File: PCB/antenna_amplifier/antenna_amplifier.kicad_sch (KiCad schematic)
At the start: 0 parts

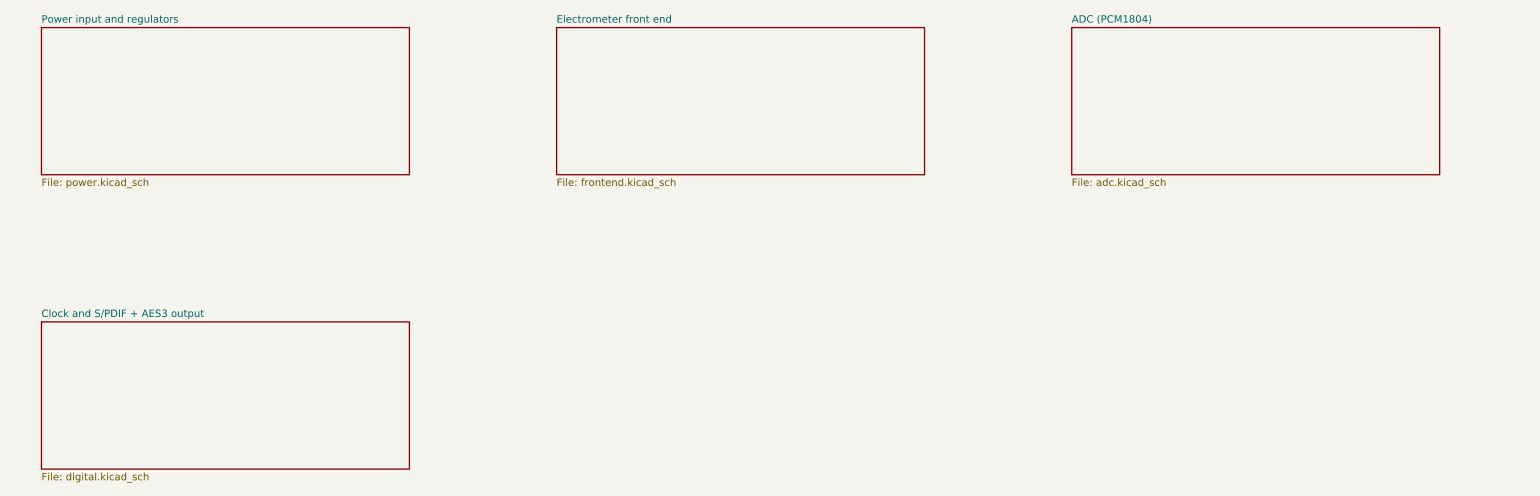
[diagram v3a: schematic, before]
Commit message: Pedantic schematic and silkscreen pass: zero overlaps, labels clear of tracks
Schematics
- tools/kicadgen/schcheck.py checks KiCad's own SVG rendering (exact stroke boxes)
  for text over text, lines through text, crowded twin labels and text outside the
  frame. Both schematics: 0 findings; ERC 0 on both.
- Generator: Sheet.join (one wire + one label instead of two facing labels),
  per-symbol field positions, per-pin stub lengths, shared power symbol for
  adjacent top/bottom rail pins, crowded rail runs get one label, longer PCM1804
  pins (no-connect cross clear of the pin number), PE value clear of its symbol.
- Fixed: doubled VIN_RAW/BIAS_DIV/LED_OVF/CV_ADJ/LED_C labels, +5VA vs VREG,
  +5V_PRE twins, CS8406 GND straps vs neighbours, BNC/LED/diode fields over their
  graphics, bucket-cell values vs tap labels, notes outside the frame, J2 -> J202.
- Root sheet: sub-sheets in signal-flow order with arrows and a design summary;
  dated title blocks.

Boards
- References prefer spots clear of tracks as well as parts (two candidate rings);
  compartment labels are re-placed after routing; the title block on the back is
  placed as one unit; no stitching via under any board text.
- DRC with schematic parity: amplifier 0 errors / 0 unconnected / 0 parity (only
  the intended bare-island mask warnings); PSU and plate 0 of anything.

Co-Authored-By: Claude Opus 5.5 <noreply@anthropic.com>
Claude-Session: https://claude.ai/code/session_01RsM1DhHhY1tSr2aHjVygSC
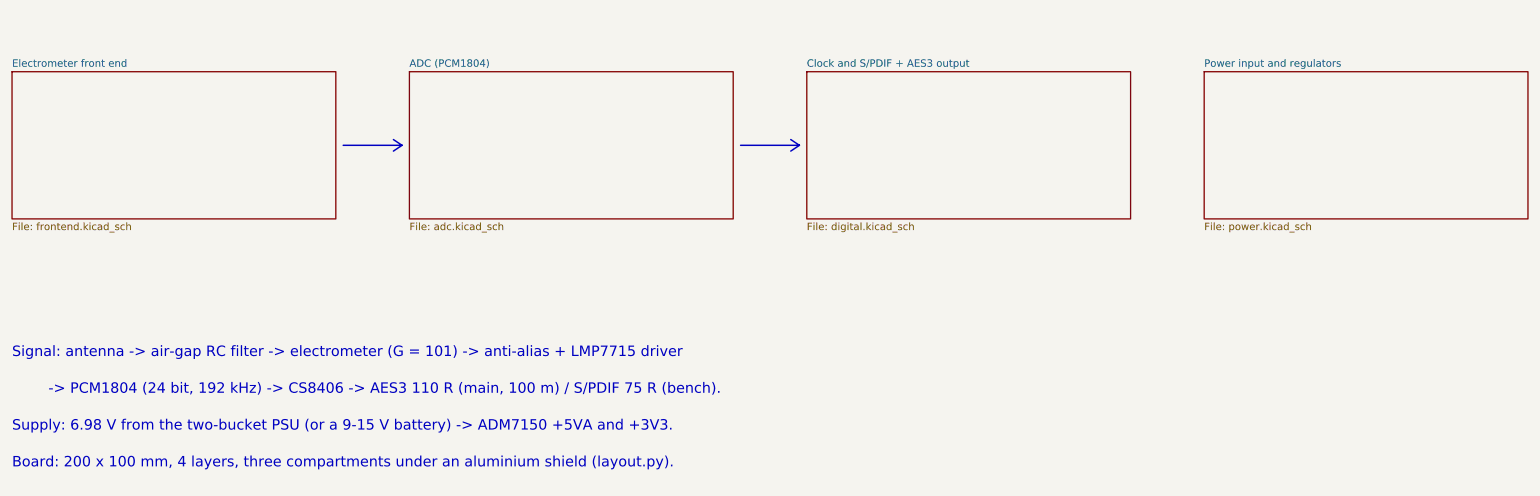
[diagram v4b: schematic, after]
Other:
- note added: "-> PCM1804 (24 bit, 192 kHz) -> CS8406 -> AES3 110 R (main, 100 m) / S/PDIF 75 R (bench)."
- note added: "Board: 200 x 100 mm, 4 layers, three compartments under an aluminium shield (layout.py)."
- note added: "Signal: antenna -> air-gap RC filter -> electrometer (G = 101) -> anti-alias + LMP7715 driver"
- note added: "Supply: 6.98 V from the two-bucket PSU (or a 9-15 V battery) -> ADM7150 +5VA and +3V3."
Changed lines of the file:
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@@
 	(title_block
 		(title "ELARA antenna amplifier")
+		(date "2026-09-30")
 		(rev "0.2")
 		(company "ELARA -- ELF Atmospheric Radio Analyser")
@@
 	)
 	(sheet
-		(at 25.4 38.1)
-		(size 63.5 25.4)
+		(at 20.32 45.72)
+		(size 55.88 25.4)
+		(exclude_from_sim no)
+		(in_bom yes)
+		(on_board yes)
+		(dnp no)
+		(fields_autoplaced yes)
+		(stroke
+			(width 0.1524)
+			(type solid)
+		)
+		(fill
+			(color 0 0 0 0)
+		)
+		(property "Sheetname" "Electrometer front end"
+			(at 20.32 45.02 0)
+			(effects
+				(font
+					(size 1.27 1.27)
+				)
+				(justify left bottom)
+			)
+		)
+		(property "Sheetfile" "frontend.kicad_sch"
+			(at 20.32 71.72 0)
+			(effects
+				(font
+					(size 1.27 1.27)
+				)
+				(justify left top)
+			)
+		)
+		(instances
+			(project "antenna_amplifier"
+				(path "/61336681-2262-5f00-9d69-45832dcbe407"
+					(page "2")
+				)
+			)
+		)
+	)
+	(polyline
+		(pts (xy 77.47 58.42) (xy 87.63 58.42))
+		(stroke
+			(width 0.254)
+			(type default)
+		)
+		(fill
+			(type none)
+		)
+	)
+	(polyline
+		(pts (xy 86.13 57.42) (xy 87.63 58.42) (xy 86.13 59.42))
+		(stroke
+			(width 0.254)
+			(type default)
+		)
+		(fill
+			(type none)
+		)
+	)
+	(sheet
+		(at 88.9 45.72)
+		(size 55.88 25.4)
+		(exclude_from_sim no)
+		(in_bom yes)
+		(on_board yes)
+		(dnp no)
+		(fields_autoplaced yes)
+		(stroke
+			(width 0.1524)
+			(type solid)
+		)
+		(fill
+			(color 0 0 0 0)
+		)
+		(property "Sheetname" "ADC (PCM1804)"
+			(at 88.9 45.02 0)
+			(effects
+				(font
+					(size 1.27 1.27)
+				)
+				(justify left bottom)
+			)
+		)
+		(property "Sheetfile" "adc.kicad_sch"
+			(at 88.9 71.72 0)
+			(effects
+				(font
+					(size 1.27 1.27)
+				)
+				(justify left top)
+			)
+		)
+		(instances
+			(project "antenna_amplifier"
+				(path "/61336681-2262-5f00-9d69-45832dcbe407"
+					(page "3")
+				)
+			)
+		)
+	)
+	(polyline
+		(pts (xy 146.05 58.42) (xy 156.21 58.42))
+		(stroke
+			(width 0.254)
+			(type default)
+		)
+		(fill
+			(type none)
+		)
+	)
+	(polyline
+		(pts (xy 154.71 57.42) (xy 156.21 58.42) (xy 154.71 59.42))
+		(stroke
+			(width 0.254)
+			(type default)
+		)
+		(fill
+			(type none)
+		)
+	)
+	(sheet
+		(at 157.48 45.72)
+		(size 55.88 25.4)
+		(exclude_from_sim no)
+		(in_bom yes)
+		(on_board yes)
+		(dnp no)
+		(fields_autoplaced yes)
+		(stroke
+			(width 0.1524)
+			(type solid)
+		)
+		(fill
+			(color 0 0 0 0)
+		)
+		(property "Sheetname" "Clock and S/PDIF + AES3 output"
+			(at 157.48 45.02 0)
+			(effects
+				(font
+					(size 1.27 1.27)
+				)
+				(justify left bottom)
+			)
+		)
+		(property "Sheetfile" "digital.kicad_sch"
+			(at 157.48 71.72 0)
+			(effects
+				(font
+					(size 1.27 1.27)
+				)
+				(justify left top)
+			)
+		)
+		(instances
+			(project "antenna_amplifier"
+				(path "/61336681-2262-5f00-9d69-45832dcbe407"
+					(page "4")
+				)
+			)
+		)
+	)
+	(sheet
+		(at 226.06 45.72)
+		(size 55.88 25.4)
 		(exclude_from_sim no)
 		(in_bom yes)
@@
 		)
 		(property "Sheetname" "Power input and regulators"
-			(at 25.4 37.4 0)
+			(at 226.06 45.02 0)
 			(effects
 				(font
@@
 		)
 		(property "Sheetfile" "power.kicad_sch"
-			(at 25.4 64.1 0)
-			(effects
-				(font
-					(size 1.27 1.27)
-				)
-				(justify left top)
-			)
-		)
-		(instances
-			(project "antenna_amplifier"
-				(path "/61336681-2262-5f00-9d69-45832dcbe407"
-					(page "2")
-				)
-			)
-		)
-	)
-	(sheet
-		(at 114.3 38.1)
-		(size 63.5 25.4)
-		(exclude_from_sim no)
-		(in_bom yes)
-		(on_board yes)
-		(dnp no)
-		(fields_autoplaced yes)
-		(stroke
-			(width 0.1524)
-			(type solid)
-		)
-		(fill
-			(color 0 0 0 0)
-		)
-		(property "Sheetname" "Electrometer front end"
-			(at 114.3 37.4 0)
-			(effects
-				(font
-					(size 1.27 1.27)
-				)
-				(justify left bottom)
-			)
-		)
-		(property "Sheetfile" "frontend.kicad_sch"
-			(at 114.3 64.1 0)
-			(effects
-				(font
-					(size 1.27 1.27)
-				)
-				(justify left top)
-			)
-		)
-		(instances
-			(project "antenna_amplifier"
-				(path "/61336681-2262-5f00-9d69-45832dcbe407"
-					(page "3")
-				)
-			)
-		)
-	)
-	(sheet
-		(at 203.2 38.1)
-		(size 63.5 25.4)
-		(exclude_from_sim no)
-		(in_bom yes)
-		(on_board yes)
-		(dnp no)
-		(fields_autoplaced yes)
-		(stroke
-			(width 0.1524)
-			(type solid)
-		)
-		(fill
-			(color 0 0 0 0)
-		)
-		(property "Sheetname" "ADC (PCM1804)"
-			(at 203.2 37.4 0)
-			(effects
-				(font
-					(size 1.27 1.27)
-				)
-				(justify left bottom)
-			)
-		)
-		(property "Sheetfile" "adc.kicad_sch"
-			(at 203.2 64.1 0)
-			(effects
-				(font
-					(size 1.27 1.27)
-				)
-				(justify left top)
-			)
-		)
-		(instances
-			(project "antenna_amplifier"
-				(path "/61336681-2262-5f00-9d69-45832dcbe407"
-					(page "4")
-				)
-			)
-		)
-	)
-	(sheet
-		(at 25.4 88.9)
-		(size 63.5 25.4)
-		(exclude_from_sim no)
-		(in_bom yes)
-		(on_board yes)
-		(dnp no)
-		(fields_autoplaced yes)
-		(stroke
-			(width 0.1524)
-			(type solid)
-		)
-		(fill
-			(color 0 0 0 0)
-		)
-		(property "Sheetname" "Clock and S/PDIF + AES3 output"
-			(at 25.4 88.2 0)
-			(effects
-				(font
-					(size 1.27 1.27)
-				)
-				(justify left bottom)
-			)
-		)
-		(property "Sheetfile" "digital.kicad_sch"
-			(at 25.4 114.9 0)
+			(at 226.06 71.72 0)
 			(effects
 				(font
@@
 		)
 	)
+	(text "Signal: antenna -> air-gap RC filter -> electrometer (G = 101) -> anti-alias + LMP7715 driver"
+		(exclude_from_sim no)
+		(at 20.32 95.25 0)
+		(effects
+			(font
+				(size 1.8 1.8)
+			)
+			(justify left bottom)
+		)
+	)
+	(text "        -> PCM1804 (24 bit, 192 kHz) -> CS8406 -> AES3 110 R (main, 100 m) / S/PDIF 75 R (bench)."
+		(exclude_from_sim no)
+		(at 20.32 101.6 0)
+		(effects
+			(font
+				(size 1.8 1.8)
+			)
+			(justify left bottom)
+		)
+	)
+	(text "Supply: 6.98 V from the two-bucket PSU (or a 9-15 V battery) -> ADM7150 +5VA and +3V3."
+		(exclude_from_sim no)
+		(at 20.32 107.95 0)
+		(effects
+			(font
+				(size 1.8 1.8)
+			)
+			(justify left bottom)
+		)
+	)
+	(text "Board: 200 x 100 mm, 4 layers, three compartments under an aluminium shield (layout.py)."
+		(exclude_from_sim no)
+		(at 20.32 114.3 0)
+		(effects
+			(font
+				(size 1.8 1.8)
+			)
+			(justify left bottom)
+		)
+	)

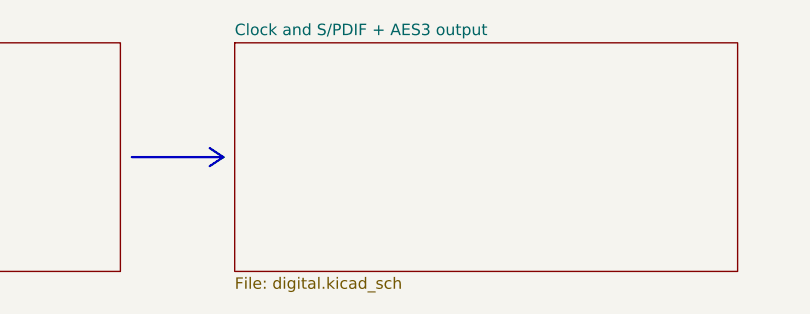
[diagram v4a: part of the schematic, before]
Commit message: Battery-friendly amplifier, RJ45 AES3 output, tidy placement, 1 mm PSU barrier
Amplifier schematic:
- No LEDs (battery use): the D301 overflow LED becomes test point TP301.
- PCM1804 FMT/S-M/OSR pins use the chip's internal 51 k pull-downs (6 resistors
  gone); BYPAS and the CS8406 mode pins get 47 k: about 3 mA less on +3V3.
- One output: AES3 on a shielded RJ45 (Amphenol RJHSE-5380, blue pair 4/5) for
  shielded twisted-pair cable, transformer isolated; the cable shield floats at
  the receiver (10 nF RF bond DNP, the DC bond is gone). The S/PDIF coax branch
  (BNC, second S22083, 5.6 mA standing current) is removed.

Layout:
- Amplifier re-placed in functional blocks on a 0.5 mm grid: PCM1804 and CS8406
  side by side so the I2S lines run straight, capacitor cells round the LDOs,
  DIP pull-downs in line with the switch pins, guard column in signal order with
  a re-routed hand guard-drive link. RJ45 notch 20 x 16 mm, BNC notch gone.
- PSU tidied (aligned columns, flyback diodes over their relays) and the charger
  / receiver copper kept >= 1.0 mm apart (was 0.30 mm): custom DRC rule, 1 mm
  router class for the relay contacts, hand-routed GND / GND_C at the relays.
- Reference labels follow each part's row; every label on silk except on the
  bare guard island. Fixed two placer bugs: each label counted as its own
  obstacle (SWIG proxies compared with 'is'), and unplaced labels blocked their
  neighbours. Texts are measured by their strokes, not KiCad's text cell.

Mechanics: RJ45 notch, plug envelope and a 1 mm isolation gap in fit_check.
BOM: 502 EUR as designed, 407 EUR recommended; 81 order lines.
Docs: STATUS, PLAN, ASSEMBLY, MOUNTING, README, mechanical and BOM notes;
MAINS_CABLE gains a certified DIY screened-cable option (H07RN-F + foil + braid)
and says why Ethernet cable must not carry mains.

All checks pass (tools/check_all.sh): ERC 0, DRC/parity 0 on all boards (only
the intended guard-island mask bridges), mains clearances, fit check, 27 tests.

Co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
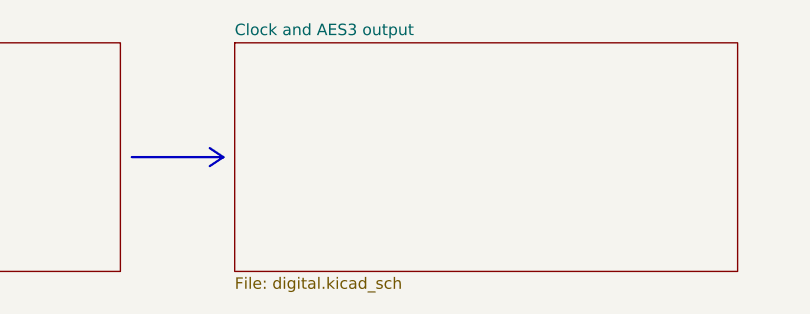
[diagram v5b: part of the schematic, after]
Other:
- sheet Clock and S/PDIF + AES3 output renamed Clock and AES3 output
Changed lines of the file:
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@@
 			(color 0 0 0 0)
 		)
-		(property "Sheetname" "Clock and S/PDIF + AES3 output"
+		(property "Sheetname" "Clock and AES3 output"
 			(at 157.48 45.02 0)
 			(effects

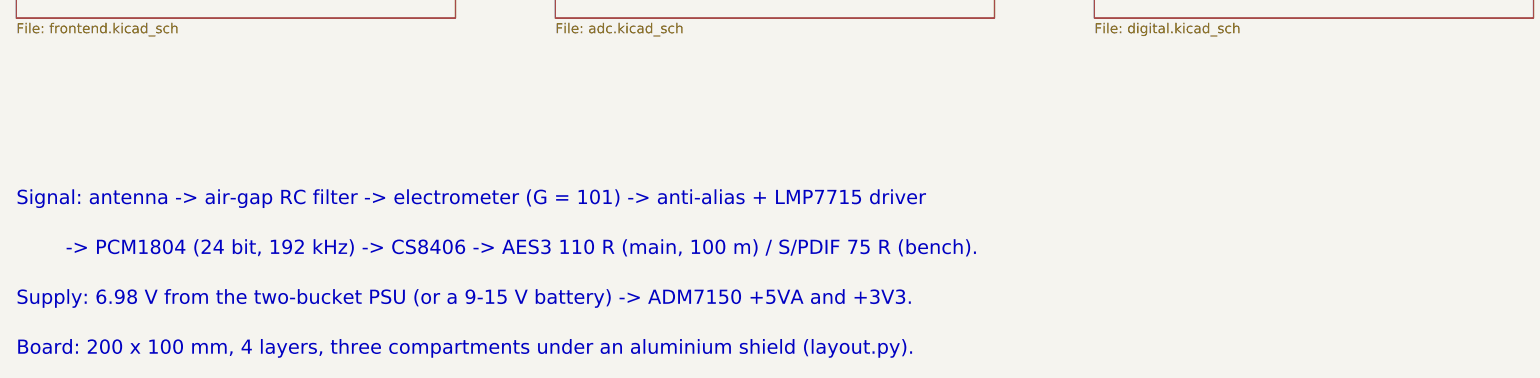
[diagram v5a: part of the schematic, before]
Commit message: AES3 source resistors 22 ohm for a 111 ohm source; tidy schematics and assembly drawings
- R412/R413 2 x 39 -> 2 x 22 ohm (Vishay TNPW060322R0BEEA, anti-sulfur): the
  CS8406 drivers are 33.5 ohm each at VL = 3.3 V, so 2 x 39 gave a 145 ohm
  source, outside AES3's 110 ohm +-20 %. The schematic note had used the 5 V
  figure and mis-added it.
- AES3 sheet: transformer flipped (kicadgen gains mirror='x') and wired straight
  to R412/R413/C405 and the RJ45, no more touching AES_HOT/AES_COLD labels.
- Stale S/PDIF and 9 V wording out of the sheets and BOM: DC input block reads
  6.98-15 V, J101 'DC IN', PSU J2 'DC OUT', reset button and clock branch say
  AES3; the legacy +9V / +9V_OUT net names are explained on the sheets.
- PSU root sheet gets the same power-path / board summary as the amplifier.
- Assembly drawings: fab-layer copies of the references removed wherever the
  silk reference shows (KiCad 9 texts cannot be hidden), so each part is named
  once; J201/J202 (no silk on the guard island) get theirs beside the part.
- BOM totals +0.14 EUR (502.15 ex VAT reference build, 407.22 recommended).

Co-Authored-By: Claude Opus 5.5 <noreply@anthropic.com>
Claude-Session: https://claude.ai/code/session_01RsM1DhHhY1tSr2aHjVygSC
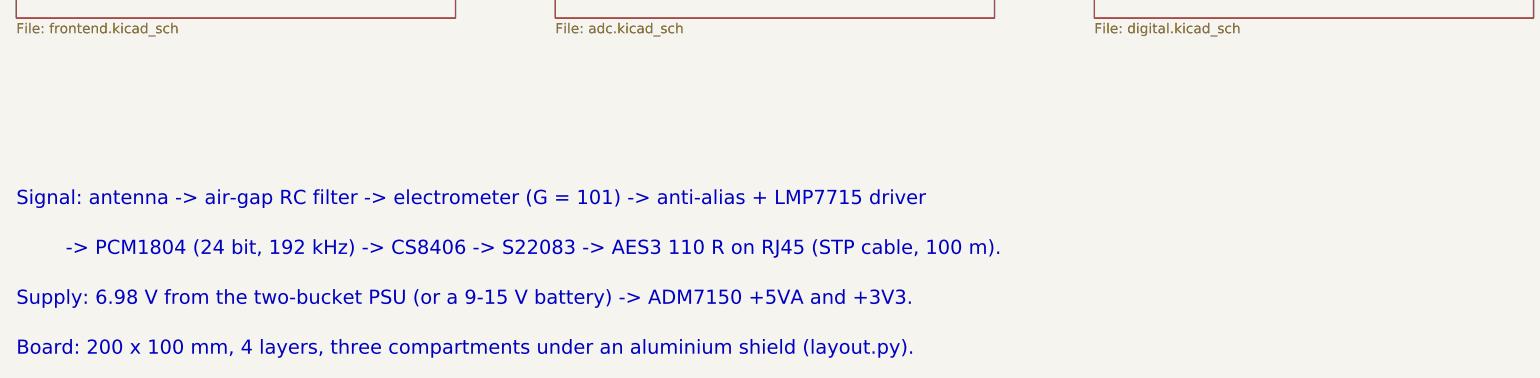
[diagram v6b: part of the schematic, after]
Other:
- note added: "-> PCM1804 (24 bit, 192 kHz) -> CS8406 -> S22083 -> AES3 110 R on RJ45 (STP cable, 100 m)."
- note removed: "-> PCM1804 (24 bit, 192 kHz) -> CS8406 -> AES3 110 R (main, 100 m) / S/PDIF 75 R (bench)."
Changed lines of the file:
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@@
 		)
 	)
-	(text "        -> PCM1804 (24 bit, 192 kHz) -> CS8406 -> AES3 110 R (main, 100 m) / S/PDIF 75 R (bench)."
+	(text "        -> PCM1804 (24 bit, 192 kHz) -> CS8406 -> S22083 -> AES3 110 R on RJ45 (STP cable, 100 m)."
 		(exclude_from_sim no)
 		(at 20.32 101.6 0)
